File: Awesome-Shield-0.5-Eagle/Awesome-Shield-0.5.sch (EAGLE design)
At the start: 17 parts, among them J1 ARDUINO_R3_SHIELDUNO_R3_SHIEL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, P1 DNP, P2 DNP, SW1 SPST_TACT-EVQQ2

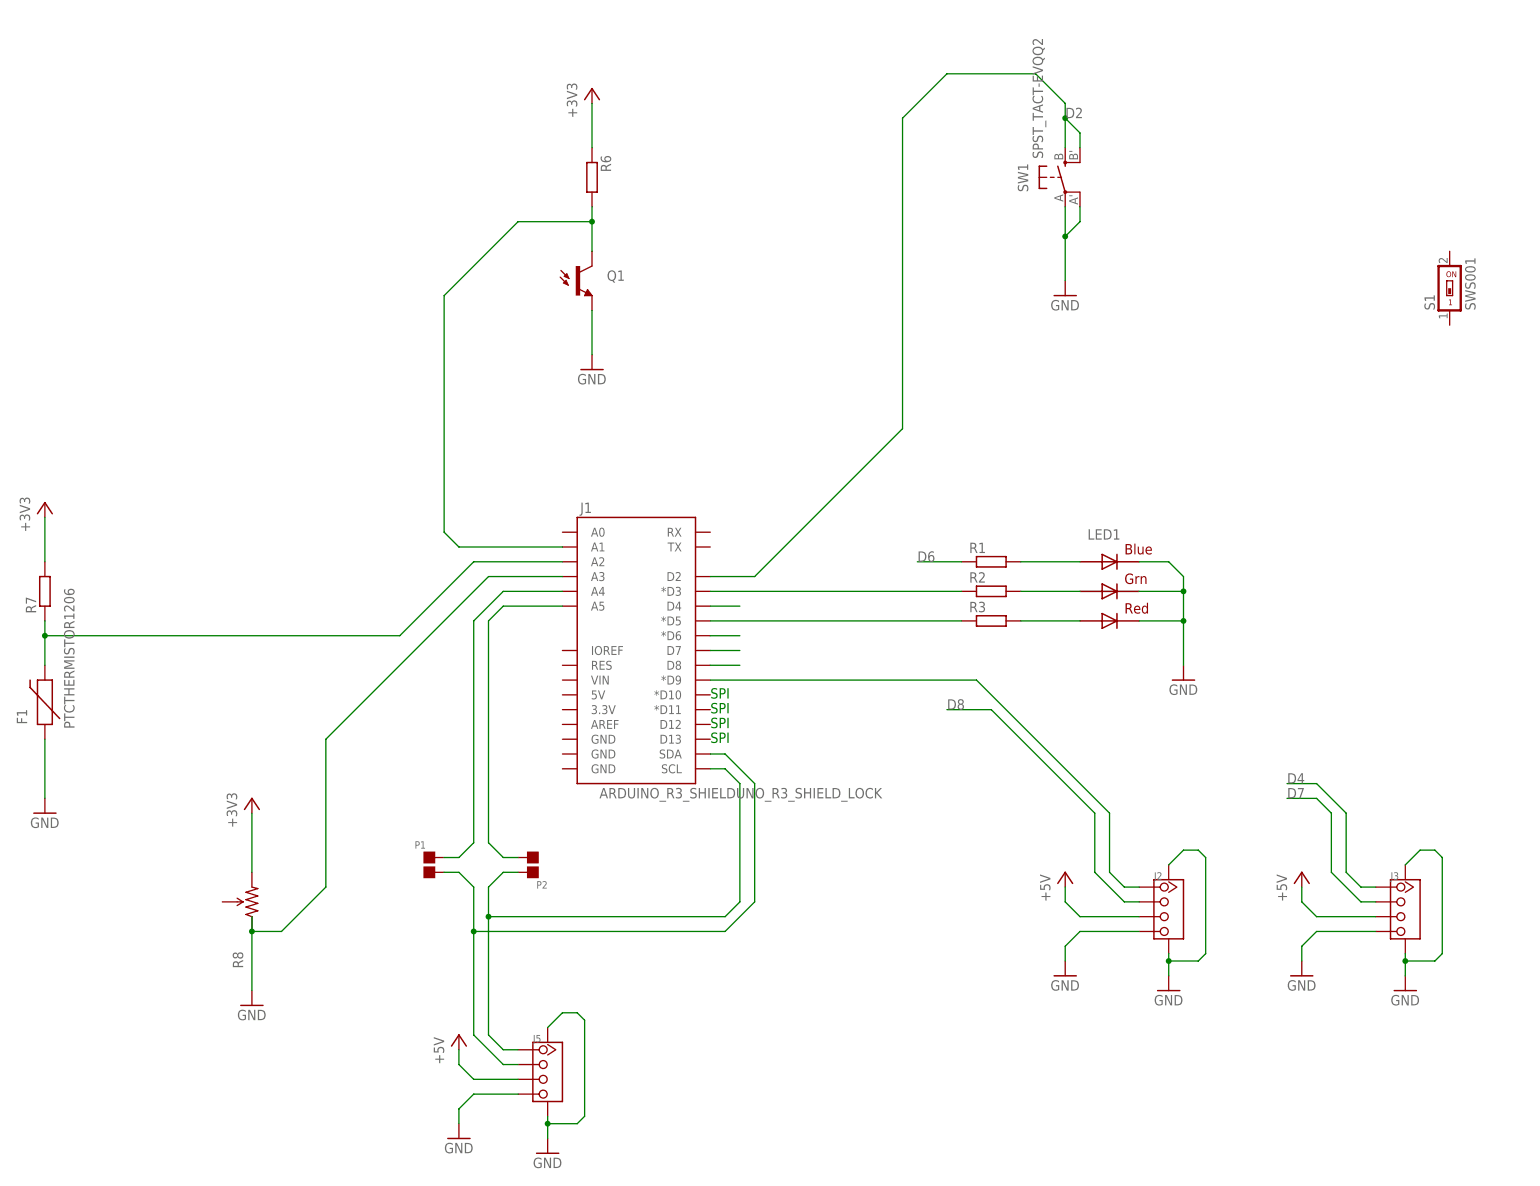
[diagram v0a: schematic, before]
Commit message: moved jumpers SDA SCL nets from A4 A5 nets
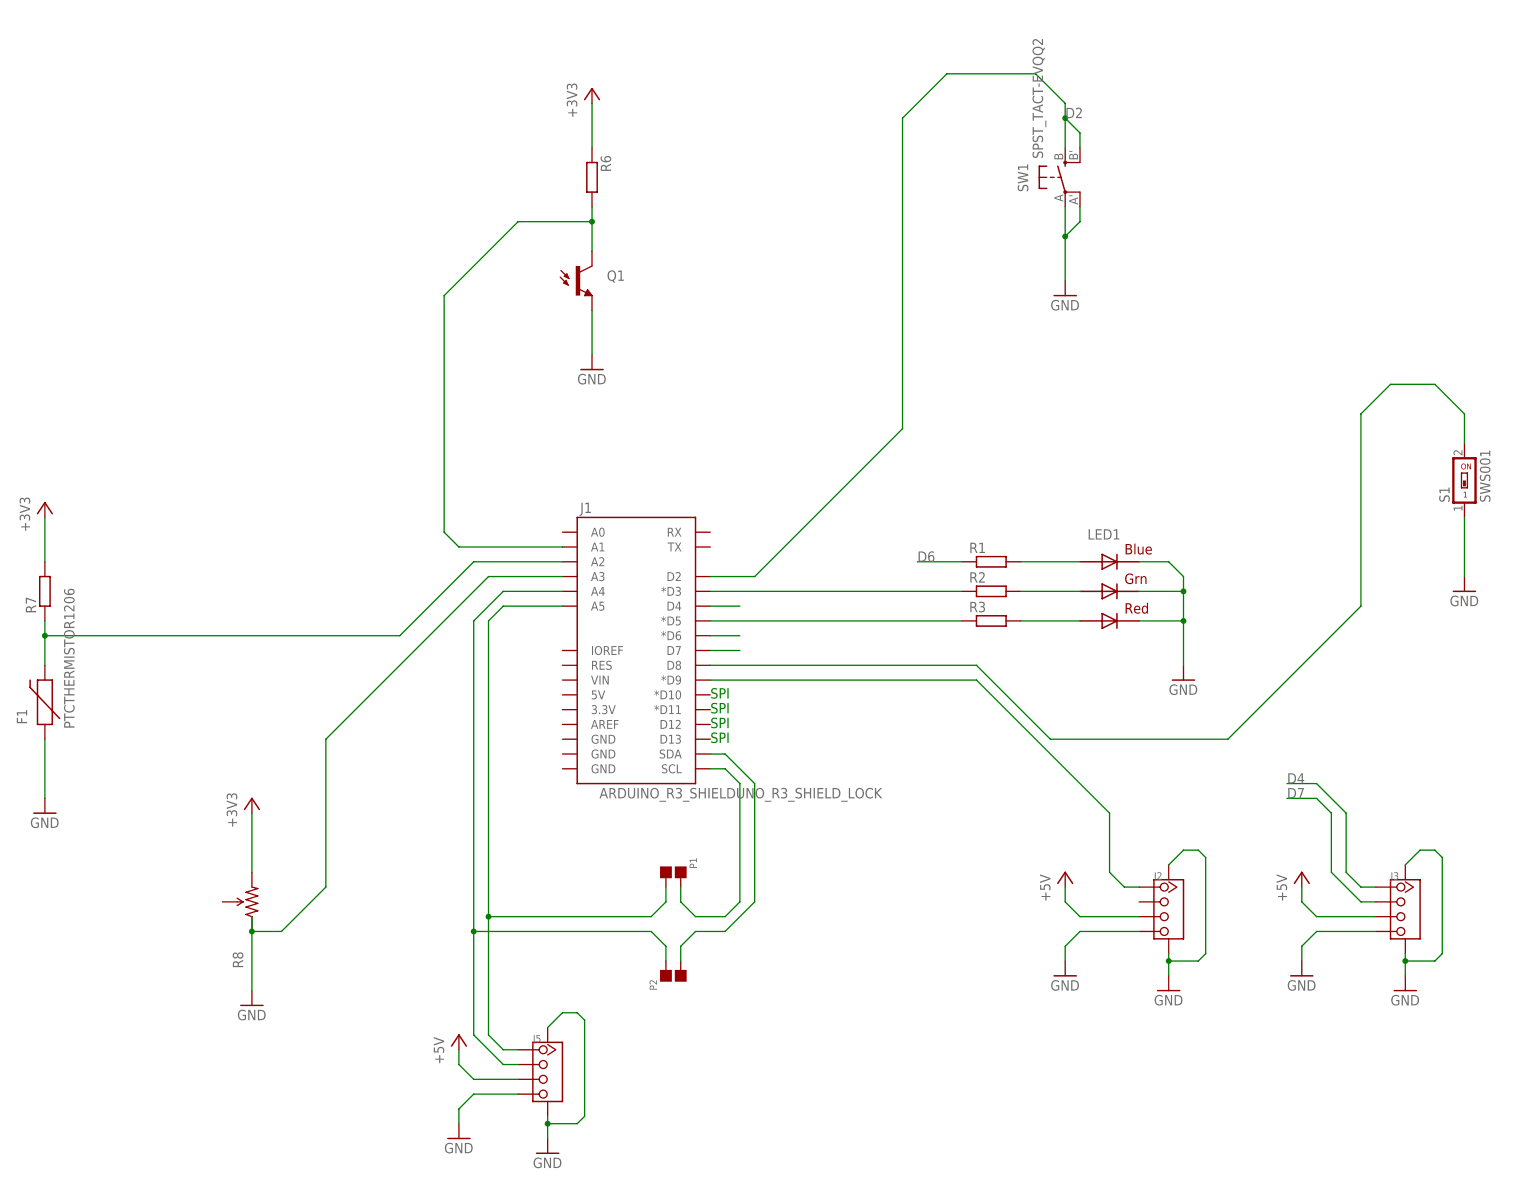
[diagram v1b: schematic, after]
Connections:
- removed net D8: J1.D8, J2.2
- new net N$1: J1.D8, S1.2
- net A4: now also J5.2, P2.2; no longer P1.2
- net A5: now also J5.1, P1.1; no longer P2.1
- net GND: now also S1.1
- net SCL: now also P1.2; no longer J5.1, P2.2
- net SDA: now also P2.1; no longer J5.2, P1.1
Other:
- moved on the sheet: P1, P2, S1
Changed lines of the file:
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@@
 <part name="P2" library="Discrete" deviceset="PAD-JUMPER-2P" device="" value="DNP"/>
 <part name="S1" library="smd-special" deviceset="SWS001" device=""/>
+<part name="GND12" library="supply1" deviceset="GND" device=""/>
 </parts>
 <sheets>
@@
 <instance part="J3" gate="G$1" x="327.66" y="85.09"/>
 <instance part="GND11" gate="1" x="327.66" y="71.12"/>
-<instance part="P1" gate="G$1" x="160.02" y="92.71"/>
-<instance part="P2" gate="G$1" x="177.8" y="92.71" rot="R180"/>
-<instance part="S1" gate="G$1" x="335.28" y="190.5"/>
+<instance part="P1" gate="G$1" x="201.93" y="91.44" rot="R270"/>
+<instance part="P2" gate="G$1" x="201.93" y="73.66" rot="R90"/>
+<instance part="S1" gate="G$1" x="337.82" y="157.48"/>
+<instance part="GND12" gate="1" x="337.82" y="139.7"/>
 </instances>
 <busses>
@@
 <wire x1="327.66" y1="76.2" x2="327.66" y2="73.66" width="0.1524" layer="91"/>
 <junction x="327.66" y="76.2"/>
+</segment>
+<segment>
+<pinref part="GND12" gate="1" pin="GND"/>
+<wire x1="337.82" y1="142.24" x2="337.82" y2="152.4" width="0.1524" layer="91"/>
+<pinref part="S1" gate="G$1" pin="1"/>
 </segment>
 </net>
@@
 <pinref part="J1" gate="G$1" pin="A4"/>
 <wire x1="172.72" y1="139.7" x2="182.88" y2="139.7" width="0.1524" layer="91"/>
-<pinref part="P1" gate="G$1" pin="2"/>
-<wire x1="165.1" y1="93.98" x2="162.56" y2="93.98" width="0.1524" layer="91"/>
-<wire x1="167.64" y1="96.52" x2="165.1" y2="93.98" width="0.1524" layer="91"/>
-<wire x1="167.64" y1="134.62" x2="167.64" y2="96.52" width="0.1524" layer="91"/>
-</segment>
-</net>
-<net name="A5" class="0">
-<segment>
-<pinref part="J1" gate="G$1" pin="A5"/>
-<wire x1="182.88" y1="137.16" x2="172.72" y2="137.16" width="0.1524" layer="91"/>
-<wire x1="172.72" y1="137.16" x2="170.18" y2="134.62" width="0.1524" layer="91"/>
-<pinref part="P2" gate="G$1" pin="1"/>
-<wire x1="170.18" y1="96.52" x2="172.72" y2="93.98" width="0.1524" layer="91"/>
-<wire x1="172.72" y1="93.98" x2="175.26" y2="93.98" width="0.1524" layer="91"/>
-<wire x1="170.18" y1="96.52" x2="170.18" y2="134.62" width="0.1524" layer="91"/>
-</segment>
-</net>
-<net name="D8" class="0">
-<segment>
-<pinref part="J1" gate="G$1" pin="D8"/>
-<wire x1="213.36" y1="127" x2="208.28" y2="127" width="0.1524" layer="91"/>
-</segment>
-<segment>
-<wire x1="281.94" y1="86.36" x2="279.4" y2="86.36" width="0.1524" layer="91"/>
-<wire x1="279.4" y1="86.36" x2="274.32" y2="91.44" width="0.1524" layer="91"/>
-<wire x1="274.32" y1="91.44" x2="274.32" y2="101.6" width="0.1524" layer="91"/>
-<wire x1="274.32" y1="101.6" x2="256.54" y2="119.38" width="0.1524" layer="91"/>
-<wire x1="256.54" y1="119.38" x2="248.92" y2="119.38" width="0.1524" layer="91"/>
-<label x="248.92" y="119.38" size="1.778" layer="95"/>
-<pinref part="J2" gate="G$1" pin="2"/>
+<wire x1="167.64" y1="134.62" x2="167.64" y2="81.28" width="0.1524" layer="91"/>
+<pinref part="J5" gate="G$1" pin="2"/>
+<wire x1="172.72" y1="58.42" x2="167.64" y2="63.5" width="0.1524" layer="91"/>
+<wire x1="172.72" y1="58.42" x2="175.26" y2="58.42" width="0.1524" layer="91"/>
+<wire x1="167.64" y1="81.28" x2="167.64" y2="63.5" width="0.1524" layer="91"/>
+<junction x="167.64" y="81.28"/>
+<pinref part="P2" gate="G$1" pin="2"/>
+<wire x1="200.66" y1="76.2" x2="200.66" y2="78.74" width="0.1524" layer="91"/>
+<wire x1="200.66" y1="78.74" x2="198.12" y2="81.28" width="0.1524" layer="91"/>
+<wire x1="198.12" y1="81.28" x2="167.64" y2="81.28" width="0.1524" layer="91"/>
 </segment>
 </net>
@@
 </segment>
 </net>
+<net name="A5" class="0">
+<segment>
+<pinref part="J5" gate="G$1" pin="1"/>
+<wire x1="170.18" y1="63.5" x2="172.72" y2="60.96" width="0.1524" layer="91"/>
+<wire x1="172.72" y1="60.96" x2="175.26" y2="60.96" width="0.1524" layer="91"/>
+<wire x1="170.18" y1="63.5" x2="170.18" y2="83.82" width="0.1524" layer="91"/>
+<junction x="170.18" y="83.82"/>
+<wire x1="200.66" y1="88.9" x2="200.66" y2="86.36" width="0.1524" layer="91"/>
+<wire x1="200.66" y1="86.36" x2="198.12" y2="83.82" width="0.1524" layer="91"/>
+<wire x1="198.12" y1="83.82" x2="170.18" y2="83.82" width="0.1524" layer="91"/>
+<pinref part="P1" gate="G$1" pin="1"/>
+<pinref part="J1" gate="G$1" pin="A5"/>
+<wire x1="182.88" y1="137.16" x2="172.72" y2="137.16" width="0.1524" layer="91"/>
+<wire x1="172.72" y1="137.16" x2="170.18" y2="134.62" width="0.1524" layer="91"/>
+<wire x1="170.18" y1="83.82" x2="170.18" y2="134.62" width="0.1524" layer="91"/>
+</segment>
+</net>
+<net name="N$1" class="0">
+<segment>
+<pinref part="J1" gate="G$1" pin="D8"/>
+<wire x1="208.28" y1="127" x2="254" y2="127" width="0.1524" layer="91"/>
+<wire x1="254" y1="127" x2="266.7" y2="114.3" width="0.1524" layer="91"/>
+<wire x1="266.7" y1="114.3" x2="297.18" y2="114.3" width="0.1524" layer="91"/>
+<wire x1="297.18" y1="114.3" x2="320.04" y2="137.16" width="0.1524" layer="91"/>
+<wire x1="320.04" y1="137.16" x2="320.04" y2="170.18" width="0.1524" layer="91"/>
+<pinref part="S1" gate="G$1" pin="2"/>
+<wire x1="337.82" y1="165.1" x2="337.82" y2="170.18" width="0.1524" layer="91"/>
+<wire x1="337.82" y1="170.18" x2="332.74" y2="175.26" width="0.1524" layer="91"/>
+<wire x1="332.74" y1="175.26" x2="325.12" y2="175.26" width="0.1524" layer="91"/>
+<wire x1="325.12" y1="175.26" x2="320.04" y2="170.18" width="0.1524" layer="91"/>
+</segment>
+</net>
+<net name="SCL" class="0">
+<segment>
+<pinref part="J1" gate="G$1" pin="SCL"/>
+<wire x1="210.82" y1="109.22" x2="208.28" y2="109.22" width="0.1524" layer="91"/>
+<wire x1="213.36" y1="106.68" x2="210.82" y2="109.22" width="0.1524" layer="91"/>
+<wire x1="213.36" y1="106.68" x2="213.36" y2="86.36" width="0.1524" layer="91"/>
+<wire x1="213.36" y1="86.36" x2="210.82" y2="83.82" width="0.1524" layer="91"/>
+<wire x1="210.82" y1="83.82" x2="205.74" y2="83.82" width="0.1524" layer="91"/>
+<wire x1="205.74" y1="83.82" x2="203.2" y2="86.36" width="0.1524" layer="91"/>
+<wire x1="203.2" y1="86.36" x2="203.2" y2="88.9" width="0.1524" layer="91"/>
+<pinref part="P1" gate="G$1" pin="2"/>
+</segment>
+</net>
 <net name="SDA" class="0">
 <segment>
@@
 <wire x1="215.9" y1="106.68" x2="215.9" y2="86.36" width="0.1524" layer="91"/>
 <wire x1="215.9" y1="86.36" x2="210.82" y2="81.28" width="0.1524" layer="91"/>
-<wire x1="210.82" y1="81.28" x2="167.64" y2="81.28" width="0.1524" layer="91"/>
-<pinref part="P1" gate="G$1" pin="1"/>
-<wire x1="162.56" y1="91.44" x2="165.1" y2="91.44" width="0.1524" layer="91"/>
-<wire x1="165.1" y1="91.44" x2="167.64" y2="88.9" width="0.1524" layer="91"/>
-<pinref part="J5" gate="G$1" pin="2"/>
-<wire x1="172.72" y1="58.42" x2="167.64" y2="63.5" width="0.1524" layer="91"/>
-<wire x1="172.72" y1="58.42" x2="175.26" y2="58.42" width="0.1524" layer="91"/>
-<wire x1="167.64" y1="88.9" x2="167.64" y2="81.28" width="0.1524" layer="91"/>
-<wire x1="167.64" y1="81.28" x2="167.64" y2="63.5" width="0.1524" layer="91"/>
-<junction x="167.64" y="81.28"/>
-</segment>
-</net>
-<net name="SCL" class="0">
-<segment>
-<pinref part="J1" gate="G$1" pin="SCL"/>
-<wire x1="210.82" y1="109.22" x2="208.28" y2="109.22" width="0.1524" layer="91"/>
-<wire x1="213.36" y1="106.68" x2="210.82" y2="109.22" width="0.1524" layer="91"/>
-<wire x1="213.36" y1="106.68" x2="213.36" y2="86.36" width="0.1524" layer="91"/>
-<wire x1="213.36" y1="86.36" x2="210.82" y2="83.82" width="0.1524" layer="91"/>
-<wire x1="210.82" y1="83.82" x2="170.18" y2="83.82" width="0.1524" layer="91"/>
-<pinref part="J5" gate="G$1" pin="1"/>
-<wire x1="170.18" y1="63.5" x2="172.72" y2="60.96" width="0.1524" layer="91"/>
-<wire x1="172.72" y1="60.96" x2="175.26" y2="60.96" width="0.1524" layer="91"/>
-<pinref part="P2" gate="G$1" pin="2"/>
-<wire x1="175.26" y1="91.44" x2="172.72" y2="91.44" width="0.1524" layer="91"/>
-<wire x1="172.72" y1="91.44" x2="170.18" y2="88.9" width="0.1524" layer="91"/>
-<wire x1="170.18" y1="63.5" x2="170.18" y2="83.82" width="0.1524" layer="91"/>
-<wire x1="170.18" y1="83.82" x2="170.18" y2="88.9" width="0.1524" layer="91"/>
-<junction x="170.18" y="83.82"/>
-</segment>
-</net>
+<wire x1="210.82" y1="81.28" x2="205.74" y2="81.28" width="0.1524" layer="91"/>
+<wire x1="205.74" y1="81.28" x2="203.2" y2="78.74" width="0.1524" layer="91"/>
+<pinref part="P2" gate="G$1" pin="1"/>
+<wire x1="203.2" y1="78.74" x2="203.2" y2="76.2" width="0.1524" layer="91"/>
+</segment>
+</net>
